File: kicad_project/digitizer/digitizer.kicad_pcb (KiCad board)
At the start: 2 copper layers, 96 x 74 mm, 63 parts, among them IC201 MAX3059ASA+T UPSTREAM, IC202 MAX6035AAUR50+T, IC203 MAX3059ASA+T DOWNSTREAM, IC204 MAX6043BAUT33+T, IC301 ADS1234IPWR, J201 DT15-4P (UPSTREAM), J202 DT06-4S (DOWNSTREAM), J301 Load Cell 1, J302 Load Cell 2, J303 Load Cell 3, J401 SHF-105-01-L-D-TH-TR, U401 ATSAM4E8EA-AN

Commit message: moved a few things around
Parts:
- moved R202 142.8 mm to (54.0, 112.5), turned to 90 degrees
- moved IC301 8.40 mm to (123.2, 104.2)
- moved IC202 8.31 mm to (140.4, 94.0), turned to 90 degrees
- moved C201 8.04 mm to (140.4, 94.2), turned to 0 degrees
- moved IC201 6.50 mm to (111.2, 94.5)
- moved IC203 6.50 mm to (99.2, 94.5)
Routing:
- net 12V_CLEAN: track 59.2 -> 52.2 mm
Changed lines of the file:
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@@
   )
   (footprint "SamacSys_Parts:SOP65P640X120-28N" (layer "F.Cu")
-    (at 131 101 90)
+    (at 123.25 104.25 90)
     (descr "PW(R-PDSO-G28)")
     (tags "Integrated Circuit")
@@
   )
   (footprint "SamacSys_Parts:SOT95P237X112-3N" (layer "F.Cu")
-    (at 144.95 101)
+    (at 140.3875 94.05 90)
     (descr "U3+1_2021")
     (tags "Integrated Circuit")
@@
     (property "Sheetname" "CANPWR")
     (attr smd)
-    (fp_text reference "IC202" (at 0 0) (layer "F.SilkS")
+    (fp_text reference "IC202" (at 0 0 90) (layer "F.SilkS")
       (effects (font (size 1.27 1.27) (thickness 0.254)))
     )
-    (fp_text value "MAX6035AAUR50+T" (at 0 0) (layer "F.SilkS") hide
+    (fp_text value "MAX6035AAUR50+T" (at 0 0 90) (layer "F.SilkS") hide
       (effects (font (size 1.27 1.27) (thickness 0.254)))
     )
-    (fp_text user "${REFERENCE}" (at 0 0) (layer "F.Fab")
+    (fp_text user "${REFERENCE}" (at 0 0 90) (layer "F.Fab")
       (effects (font (size 1.27 1.27) (thickness 0.254)))
     )
@@
     (fp_line (start 0.65 -1.46) (end 0.65 1.46) (layer "F.Fab") (width 0.1))
     (fp_line (start 0.65 1.46) (end -0.65 1.46) (layer "F.Fab") (width 0.1))
-    (pad "1" smd rect locked (at -1.05 -0.95 90) (size 0.6 1.3) (layers "F.Cu" "F.Paste" "F.Mask")
+    (pad "1" smd rect locked (at -1.05 -0.95 180) (size 0.6 1.3) (layers "F.Cu" "F.Paste" "F.Mask")
       (net 149 "12V_CLEAN") (pinfunction "IN") (pintype "power_in"))
-    (pad "2" smd rect locked (at -1.05 0.95 90) (size 0.6 1.3) (layers "F.Cu" "F.Paste" "F.Mask")
+    (pad "2" smd rect locked (at -1.05 0.95 180) (size 0.6 1.3) (layers "F.Cu" "F.Paste" "F.Mask")
       (net 2 "5V_CLEAN") (pinfunction "OUT") (pintype "power_out"))
-    (pad "3" smd rect locked (at 1.05 0 90) (size 0.6 1.3) (layers "F.Cu" "F.Paste" "F.Mask")
+    (pad "3" smd rect locked (at 1.05 0 180) (size 0.6 1.3) (layers "F.Cu" "F.Paste" "F.Mask")
       (net 1 "GND") (pinfunction "GND") (pintype "power_in"))
     (model "C:\\Users\\short\\Documents\\KiCad\\SamacSys_Parts.3dshapes\\MAX6035AAUR50+T.stp"
@@
   )
   (footprint "Resistor_SMD:R_2512_6332Metric_Pad1.40x3.35mm_HandSolder" (layer "F.Cu")
-    (at 192.675 78.32)
+    (at 54 112.55 90)
     (descr "Resistor SMD 2512 (6332 Metric), square (rectangular) end terminal, IPC_7351 nominal with elongated pad for handsoldering. (Body size source: IPC-SM-782 page 72, https://www.pcb-3d.com/wordpress/wp-content/uploads/ipc-sm-782a_amendment_1_and_2.pdf), generated with kicad-footprint-generator")
     (tags "resistor handsolder")
@@
     (property "Sheetname" "CANPWR")
     (attr smd)
-    (fp_text reference "R202" (at 0 -2.62) (layer "F.SilkS")
+    (fp_text reference "R202" (at 0 -2.62 90) (layer "F.SilkS")
       (effects (font (size 1 1) (thickness 0.15)))
     )
-    (fp_text value "50k" (at 0 2.62) (layer "F.Fab")
+    (fp_text value "50k" (at 0 2.62 90) (layer "F.Fab")
       (effects (font (size 1 1) (thickness 0.15)))
     )
-    (fp_text user "${REFERENCE}" (at 0 0) (layer "F.Fab")
+    (fp_text user "${REFERENCE}" (at 0 0 90) (layer "F.Fab")
       (effects (font (size 1 1) (thickness 0.15)))
     )
@@
     (fp_line (start -3.15 1.6) (end -3.15 -1.6) (layer "F.Fab") (width 0.1))
     (fp_line (start 3.15 -1.6) (end 3.15 1.6) (layer "F.Fab") (width 0.1))
-    (pad "1" smd roundrect locked (at -3.05 0) (size 1.4 3.35) (layers "F.Cu" "F.Paste" "F.Mask") (roundrect_rratio 0.178571)
+    (pad "1" smd roundrect locked (at -3.05 0 90) (size 1.4 3.35) (layers "F.Cu" "F.Paste" "F.Mask") (roundrect_rratio 0.178571)
       (net 1 "GND") (pintype "passive"))
-    (pad "2" smd roundrect locked (at 3.05 0) (size 1.4 3.35) (layers "F.Cu" "F.Paste" "F.Mask") (roundrect_rratio 0.178571)
+    (pad "2" smd roundrect locked (at 3.05 0 90) (size 1.4 3.35) (layers "F.Cu" "F.Paste" "F.Mask") (roundrect_rratio 0.178571)
       (net 20 "Net-(IC203-Pad8)") (pintype "passive"))
     (model "${KICAD6_3DMODEL_DIR}/Resistor_SMD.3dshapes/R_2512_6332Metric.wrl"
@@
   )
   (footprint "SamacSys_Parts:SOIC127P600X175-8N" (layer "F.Cu")
-    (at 111 101)
+    (at 111.25 94.5)
     (descr "S8+4")
     (tags "Integrated Circuit")
@@
   )
   (footprint "SamacSys_Parts:SOIC127P600X175-8N" (layer "F.Cu")
-    (at 99 101 180)
+    (at 99.25 94.5 180)
     (descr "S8+4")
     (tags "Integrated Circuit")
@@
   )
   (footprint "Capacitor_SMD:C_2220_5650Metric_Pad1.97x5.40mm_HandSolder" (layer "B.Cu")
-    (at 144.75 101 -90)
+    (at 140.3875 94.25)
     (descr "Capacitor SMD 2220 (5650 Metric), square (rectangular) end terminal, IPC_7351 nominal with elongated pad for handsoldering. (Body size from: http://datasheets.avx.com/AVX-HV_MLCC.pdf), generated with kicad-footprint-generator")
     (tags "capacitor handsolder")
@@
     (property "Sheetname" "CANPWR")
     (attr smd)
-    (fp_text reference "C201" (at 0 3.65 90) (layer "B.SilkS")
+    (fp_text reference "C201" (at 0 3.65) (layer "B.SilkS")
       (effects (font (size 1 1) (thickness 0.15)) (justify mirror))
     )
-    (fp_text value "0.1uF" (at 0 -3.65 90) (layer "B.Fab")
+    (fp_text value "0.1uF" (at 0 -3.65) (layer "B.Fab")
       (effects (font (size 1 1) (thickness 0.15)) (justify mirror))
     )
-    (fp_text user "${REFERENCE}" (at 0 0 90) (layer "B.Fab")
+    (fp_text user "${REFERENCE}" (at 0 0) (layer "B.Fab")
       (effects (font (size 1 1) (thickness 0.15)) (justify mirror))
     )
@@
     (fp_line (start -2.85 2.5) (end 2.85 2.5) (layer "B.Fab") (width 0.1))
     (fp_line (start -2.85 -2.5) (end -2.85 2.5) (layer "B.Fab") (width 0.1))
-    (pad "1" smd roundrect locked (at -2.6375 0 270) (size 1.975 5.4) (layers "B.Cu" "B.Paste" "B.Mask") (roundrect_rratio 0.126582)
+    (pad "1" smd roundrect locked (at -2.6375 0) (size 1.975 5.4) (layers "B.Cu" "B.Paste" "B.Mask") (roundrect_rratio 0.126582)
       (net 149 "12V_CLEAN") (pintype "passive"))
-    (pad "2" smd roundrect locked (at 2.6375 0 270) (size 1.975 5.4) (layers "B.Cu" "B.Paste" "B.Mask") (roundrect_rratio 0.126582)
+    (pad "2" smd roundrect locked (at 2.6375 0) (size 1.975 5.4) (layers "B.Cu" "B.Paste" "B.Mask") (roundrect_rratio 0.126582)
       (net 1 "GND") (pintype "passive"))
     (model "${KICAD6_3DMODEL_DIR}/Capacitor_SMD.3dshapes/C_2220_5650Metric.wrl"
@@
   (gr_line (start 170.25 119.25) (end 170.25 52.75) (layer "Edge.Cuts") (width 0.1))
   (gr_arc (start 166.5 49) (mid 169.15165 50.09835) (end 170.25 52.75) (layer "Edge.Cuts") (width 0.1))
-  (segment (start 146 101) (end 146 102.3875) (width 0.25) (layer "F.Cu") (net 1))
-  (segment (start 146 102.3875) (end 144.75 103.6375) (width 0.25) (layer "F.Cu") (net 1))
+  (segment (start 140.3875 93) (end 141.775 93) (width 0.25) (layer "F.Cu") (net 1))
+  (segment (start 141.775 93) (end 143.025 94.25) (width 0.25) (layer "F.Cu") (net 1))
   (segment (start 116 54.75) (end 116 53.5) (width 0.25) (layer "F.Cu") (net 1))
   (via (at 116 53.5) (size 0.8) (drill 0.4) (layers "F.Cu" "B.Cu") (net 1))
-  (via (at 144.75 103.6375) (size 0.8) (drill 0.4) (layers "F.Cu" "B.Cu") (net 1))
+  (via (at 143.025 94.25) (size 0.8) (drill 0.4) (layers "F.Cu" "B.Cu") (net 1))
   (segment (start 92.87 53.32) (end 91.5 51.95) (width 0.25) (layer "F.Cu") (net 37))
   (segment (start 92.87 55) (end 92.87 53.32) (width 0.25) (layer "F.Cu") (net 37))
-  (segment (start 143.9 100.05) (end 143.9 99.2125) (width 0.25) (layer "F.Cu") (net 149))
+  (segment (start 139.4375 95.1) (end 138.6 95.1) (width 0.25) (layer "F.Cu") (net 149))
+  (segment (start 137.75 94.25) (end 137.6 94.1) (width 0.25) (layer "F.Cu") (net 149))
   (segment (start 115.05 57.825) (end 116 58.775) (width 0.25) (layer "F.Cu") (net 149))
-  (segment (start 143.9 99.2125) (end 144.75 98.3625) (width 0.25) (layer "F.Cu") (net 149))
-  (segment (start 144.75 98.3625) (end 137.6 91.2125) (width 0.25) (layer "F.Cu") (net 149))
+  (segment (start 138.6 95.1) (end 137.75 94.25) (width 0.25) (layer "F.Cu") (net 149))
   (segment (start 116 58.775) (end 131.235 74.01) (width 0.25) (layer "F.Cu") (net 149))
+  (segment (start 137.6 94.1) (end 137.6 74.01) (width 0.25) (layer "F.Cu") (net 149))
   (segment (start 131.235 74.01) (end 137.6 74.01) (width 0.25) (layer "F.Cu") (net 149))
-  (segment (start 137.6 91.2125) (end 137.6 74.01) (width 0.25) (layer "F.Cu") (net 149))
   (segment (start 115.05 57.25) (end 115.05 57.825) (width 0.25) (layer "F.Cu") (net 149))
   (via (at 116 58.775) (size 0.8) (drill 0.4) (layers "F.Cu" "B.Cu") (net 149))
-  (via (at 144.75 98.3625) (size 0.8) (drill 0.4) (layers "F.Cu" "B.Cu") (net 149))
+  (via (at 137.75 94.25) (size 0.8) (drill 0.4) (layers "F.Cu" "B.Cu") (net 149))
   (zone (net 3) (net_name "3V3_CLEAN") (layer "F.Cu") (name "3V3_CLEAN_PLANE") (hatch edge 0.508)
     (connect_pads (clearance 0.254))

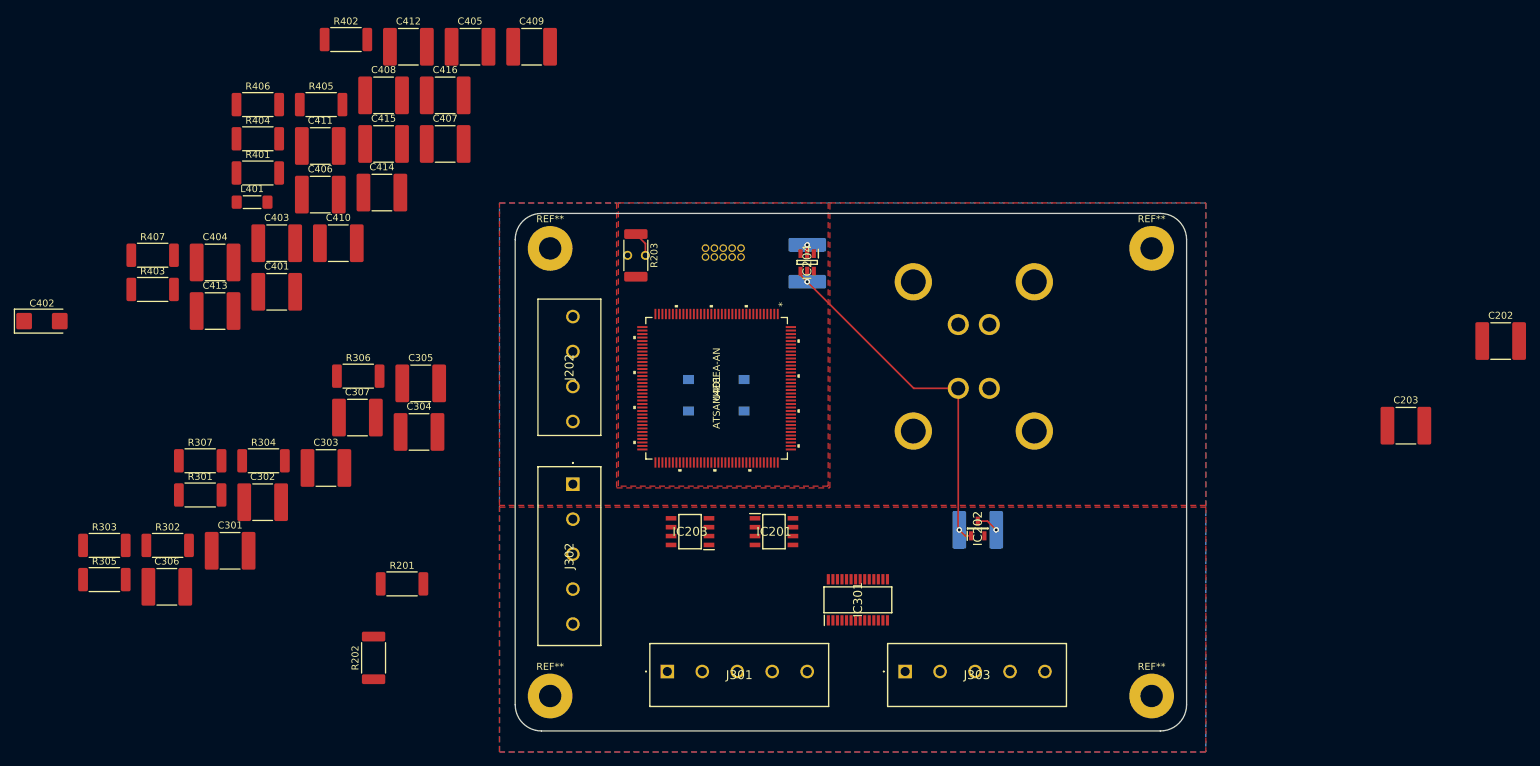
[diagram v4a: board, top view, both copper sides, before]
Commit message: finished ADC routing, including MCU pins (MUX, I2C, etc.)
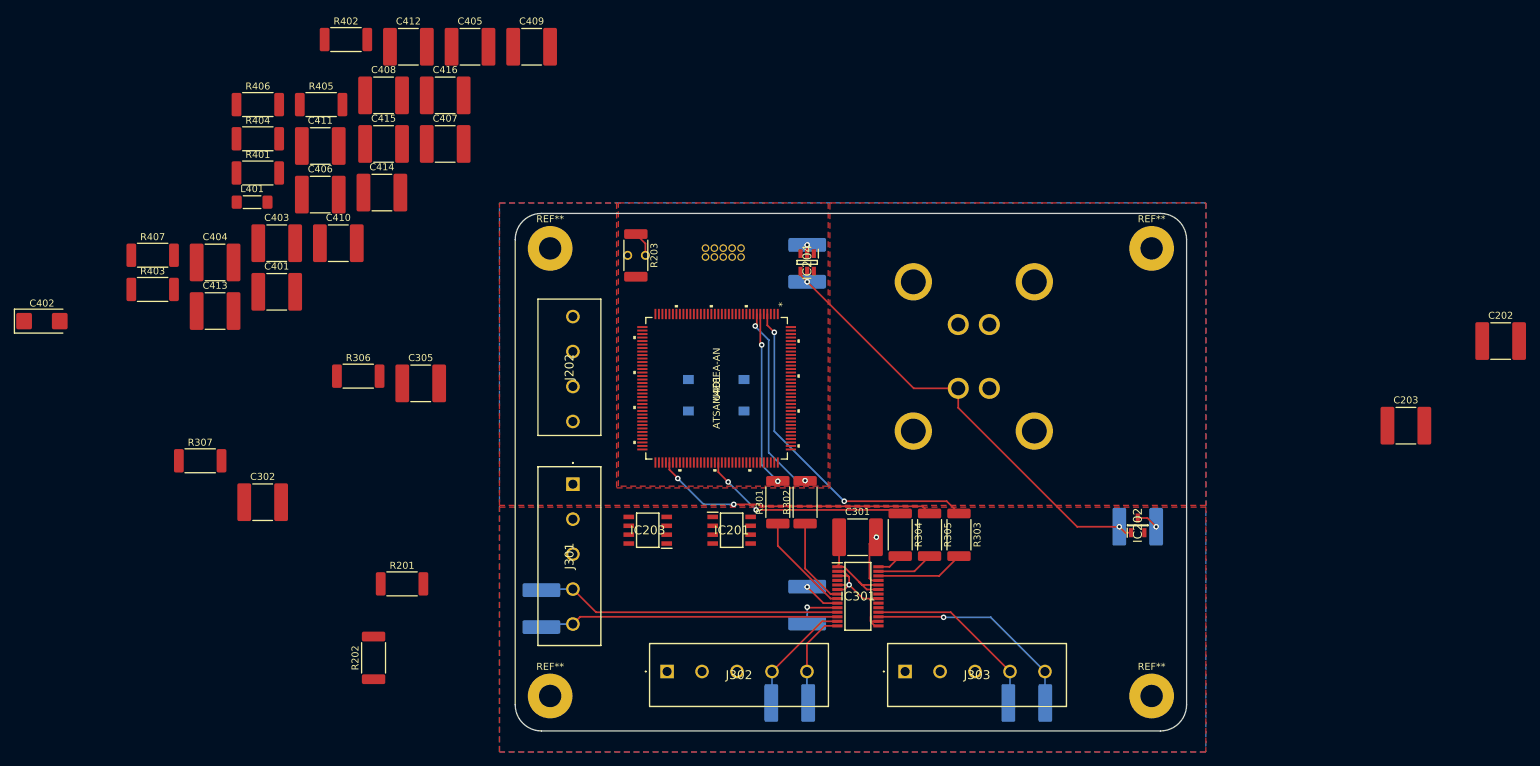
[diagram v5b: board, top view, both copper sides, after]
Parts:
- C303, C304, C306, C307: moved to B.Cu
- moved R303 122.2 mm to (137.7, 95.0), turned to -90 degrees
- moved R305 118.2 mm to (133.5, 95.0), turned to -90 degrees
- moved C304 95.1 mm to (147.4, 119.0), turned to 180 degrees
- moved R304 91.7 mm to (129.3, 95.0), turned to -90 degrees
- moved R302 91.3 mm to (115.7, 90.3), turned to 90 degrees
- moved C301 89.7 mm to (123.2, 95.3)
- moved R301 82.6 mm to (111.8, 90.3), turned to 90 degrees
- moved C307 74.1 mm to (113.5, 119.0)
- moved C303 71.5 mm to (116.0, 105.0), turned to -90 degrees
- moved C306 53.7 mm to (78.0, 105.5), turned to -90 degrees
- moved J301 30.0 mm to (82.5, 87.7), turned to -90 degrees
- moved J302 30.0 mm to (96.0, 114.5), turned to 0 degrees
- moved C201 22.9 mm to (163.3, 93.8)
- moved IC202 22.9 mm to (163.3, 93.6)
- moved IC201 6.05 mm to (105.2, 94.3)
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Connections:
- C304 pad 1: /ANALOG/signal (-) -> /ANALOG/load cell 3 - signal (-)
- C304 pad 2: /ANALOG/signal (+) -> /ANALOG/load cell 3 - signal (+)
- C306 pad 1: /ANALOG/signal (+) -> /ANALOG/load cell 1 - signal (+)
- C306 pad 2: /ANALOG/signal (-) -> /ANALOG/load cell 1 - signal (-)
- C307 pad 1: /ANALOG/signal (+) -> /ANALOG/load cell 2 - signal (+)
- C307 pad 2: /ANALOG/signal (-) -> /ANALOG/load cell 2 - signal (-)
- IC301 pad 11: /ANALOG/signal (+) -> /ANALOG/load cell 1 - signal (+)
- IC301 pad 12: /ANALOG/signal (-) -> /ANALOG/load cell 1 - signal (-)
- IC301 pad 13: /ANALOG/signal (+) -> /ANALOG/load cell 2 - signal (+)
- IC301 pad 14: /ANALOG/signal (-) -> /ANALOG/load cell 2 - signal (-)
- IC301 pad 17: /ANALOG/signal (-) -> /ANALOG/load cell 3 - signal (-)
- IC301 pad 18: /ANALOG/signal (+) -> /ANALOG/load cell 3 - signal (+)
- J301 pad 4: /ANALOG/signal (+) -> /ANALOG/load cell 1 - signal (+)
- J301 pad 5: /ANALOG/signal (-) -> /ANALOG/load cell 1 - signal (-)
- J302 pad 4: /ANALOG/signal (+) -> /ANALOG/load cell 2 - signal (+)
- J302 pad 5: /ANALOG/signal (-) -> /ANALOG/load cell 2 - signal (-)
- J303 pad 4: /ANALOG/signal (+) -> /ANALOG/load cell 3 - signal (+)
- J303 pad 5: /ANALOG/signal (-) -> /ANALOG/load cell 3 - signal (-)
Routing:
- net ADC_nPWDN: track 0.00 -> 48.5 mm, vias 0 -> 2
- net /ANALOG/load cell 1 - signal (+): track 0.00 -> 43.7 mm
- net /ANALOG/load cell 1 - signal (-): track 0.00 -> 42.9 mm
- net I2C_SCL: track 0.00 -> 40.9 mm, vias 0 -> 2
- net /ANALOG/load cell 3 - signal (-): track 0.00 -> 31.6 mm, vias 0 -> 1
- net I2C_SDA: track 0.00 -> 29.8 mm, vias 0 -> 2
- net GND: track 4.41 -> 32.5 mm, vias 2 -> 4
- net ADC_MUX_1: track 0.00 -> 27.6 mm, vias 0 -> 2
- net /ANALOG/load cell 3 - signal (+): track 0.00 -> 26.9 mm
- net ADC_MUX_0: track 0.00 -> 25.0 mm, vias 0 -> 2
- net /ANALOG/load cell 2 - signal (+): track 0.00 -> 16.9 mm
- net Net-(IC301-Pad8): track 0.00 -> 15.2 mm
- net 3V3_CLEAN: track 0.00 -> 14.4 mm
- net /ANALOG/load cell 2 - signal (-): track 0.00 -> 13.9 mm
- net Net-(IC301-Pad7): track 0.00 -> 12.9 mm
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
